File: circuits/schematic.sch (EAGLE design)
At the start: 38 parts, among them IC1 MEGA8-P, IC2 MAX481CPA, J1 AVR_SPI_PRG_6PTH

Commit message: Circuit layout v1.
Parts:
- added R14, R15, R16, R17: (no value), SparkFun-Passives:RESISTORPTH-1/4W
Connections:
- removed net N$14: IC1.PB2(SS/OC1B), R4.1
- removed net N$37: IC1.PD6(AIN0), JP2.6
- removed net N$38: R11.2, U$12.B
- removed net N$44: IC1.PC4(ADC4/SDA), R12.1
- removed net N$46: IC1.PD7(AIN1), JP4.6
- removed net N$49: IC1.PC3(ADC3), R11.1
- new net N$50: IC1.PC5(ADC5/SCL), R16.1
- new net N$51: JP4.3, U$12.C
- new net N$52: JP4.5, U$13.C
- new net N$53: JP4.4, U$14.C
- new net N$54: IC1.PB3(MOSI/OC2), J1.4, R3.1
- new net N$55: IC1.PB4(MISO), J1.1, R4.1
- net GND: now also J1.6, R13.2, R17.2, R2.2, R9.2, U$10.E, U$11.E, U$12.E, U$13.E, U$14.E, U$3.E, U$4.E, U$5.E, U$6.E, U$7.E, U$8.E, U$9.E; no longer JP1.1, JP1.2, JP2.1, JP2.2, JP3.1, JP3.2, JP4.1, JP4.2
- net N$10: now also JP1.4, U$8.C; no longer JP3.5, U$4.E
- net N$11: now also IC1.PC4(ADC4/SDA), R15.1; no longer JP3.4, U$5.E
- net N$12: now also R5.1; no longer R2.1
- net N$13: now also R6.1; no longer R3.1
- net N$15: now also JP1.6, R2.1; no longer JP3.6
- net N$21: now also IC1.PD5(T1), JP2.6, R9.1; no longer JP1.3, U$6.E
- net N$23: now also R3.2, U$3.B; no longer JP1.5, U$7.E
- net N$24: now also R4.2, U$4.B; no longer JP1.4, U$8.E
- net N$25: now also U$5.B; no longer U$9.B
- net N$26: now also IC1.PB5(SCK), J1.3, R8.1; no longer IC1.PB4(MISO), R6.1
- net N$27: now also IC1.PB2(SS/OC1B); no longer IC1.PB5(SCK)
- net N$28: now also JP2.3, U$3.C; no longer R4.2, U$5.B
- net N$29: now also JP2.5, U$4.C; no longer IC1.PD5(T1), JP1.6
- net N$3: now also IC1.PC3(ADC3), R14.1; no longer R2.2, U$3.B
- net N$30: now also JP2.4, U$5.C; no longer R9.2, U$10.B
- net N$31: now also IC1.PD6(AIN0), JP3.6, R13.1; no longer R10.2, U$11.B
- net N$32: now also R10.2, U$9.B; no longer JP2.3, U$9.E
- net N$33: now also R11.2, U$10.B; no longer JP2.5, U$10.E
- net N$34: now also R12.2, U$11.B; no longer JP2.4, U$11.E
- net N$35: now also R11.1; no longer R9.1
- net N$36: now also R12.1; no longer R10.1
- net N$39: now also JP3.3, U$9.C; no longer R12.2, U$13.B
- net N$40: now also JP3.5, U$10.C; no longer R13.2, U$14.B
- net N$41: now also JP3.4, U$11.C; no longer JP4.3, U$12.E
- net N$42: now also IC1.PD7(AIN1), JP4.6, R17.1; no longer JP4.5, U$13.E
- net N$43: now also R14.2, U$12.B; no longer JP4.4, U$14.E
- net N$45: now also R15.2, U$13.B; no longer IC1.PC5(ADC5/SCL), R13.1
- net N$47: now also R16.2, U$14.B; no longer IC1.PB3(MOSI/OC2), R5.1
- net N$48: now also R10.1; no longer R8.1
- net N$6: now also JP1.3, U$6.C; no longer R3.2, U$4.B
- net N$9: now also JP1.5, U$7.C; no longer JP3.3, U$3.E
- net VCC: now also JP1.1, JP1.2, JP2.1, JP2.2, JP3.1, JP3.2, JP4.1, JP4.2; no longer U$10.C, U$11.C, U$12.C, U$13.C, U$14.C, U$3.C, U$4.C, U$5.C, U$6.C, U$7.C, U$8.C, U$9.C
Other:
- moved on the sheet: JP1, JP2, JP3, JP4, R10, R11, R12, R13, R2, R3, R4, R5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

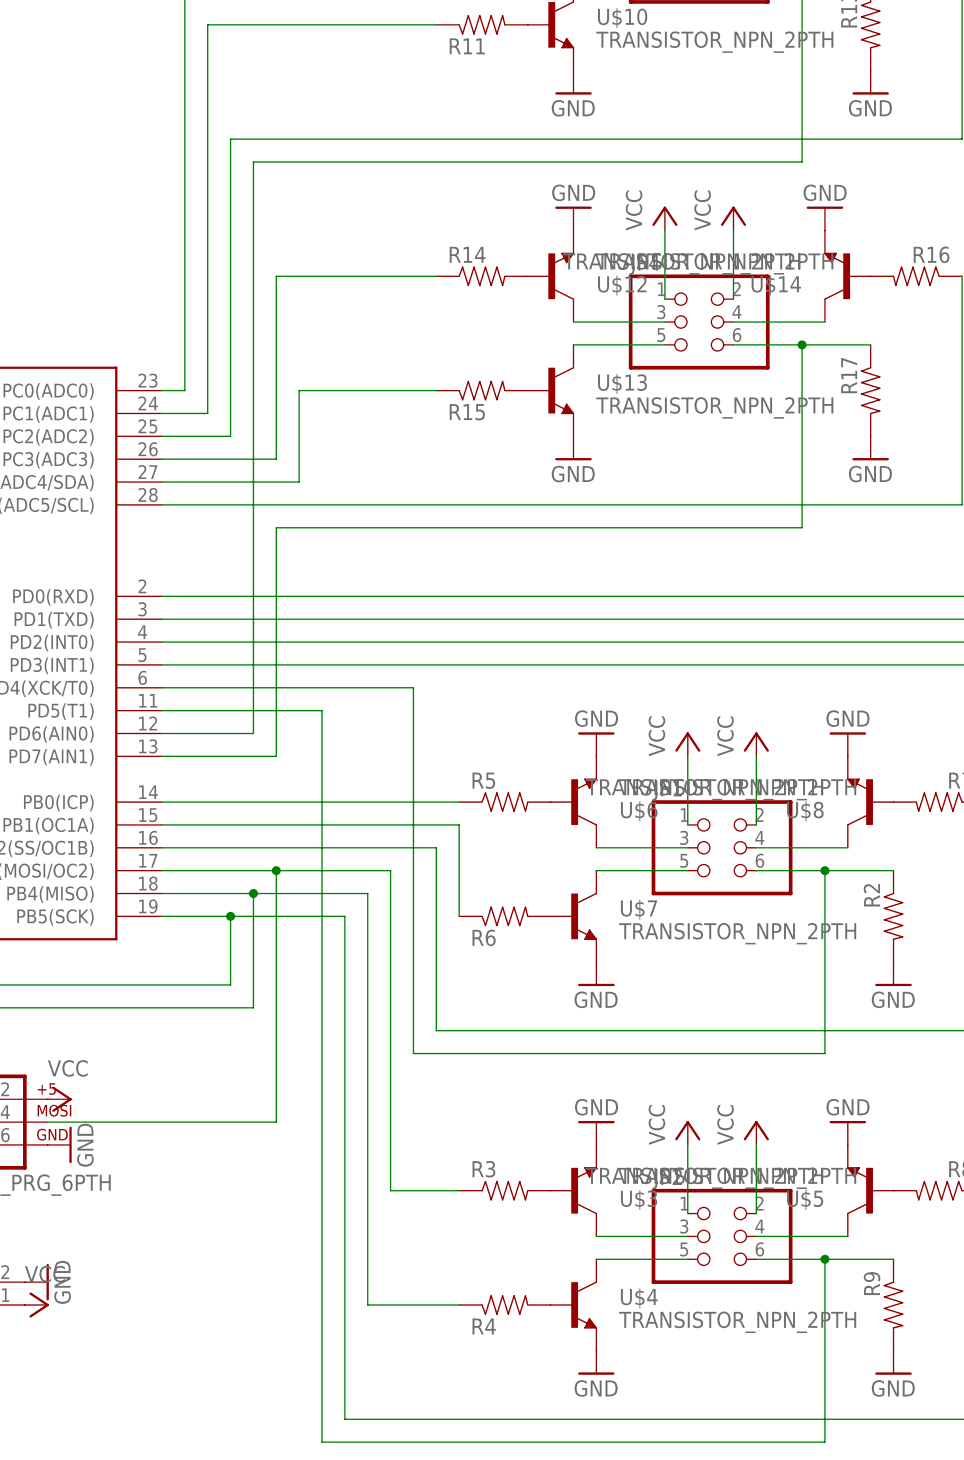
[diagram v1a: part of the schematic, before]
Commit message: Inverted switch order.
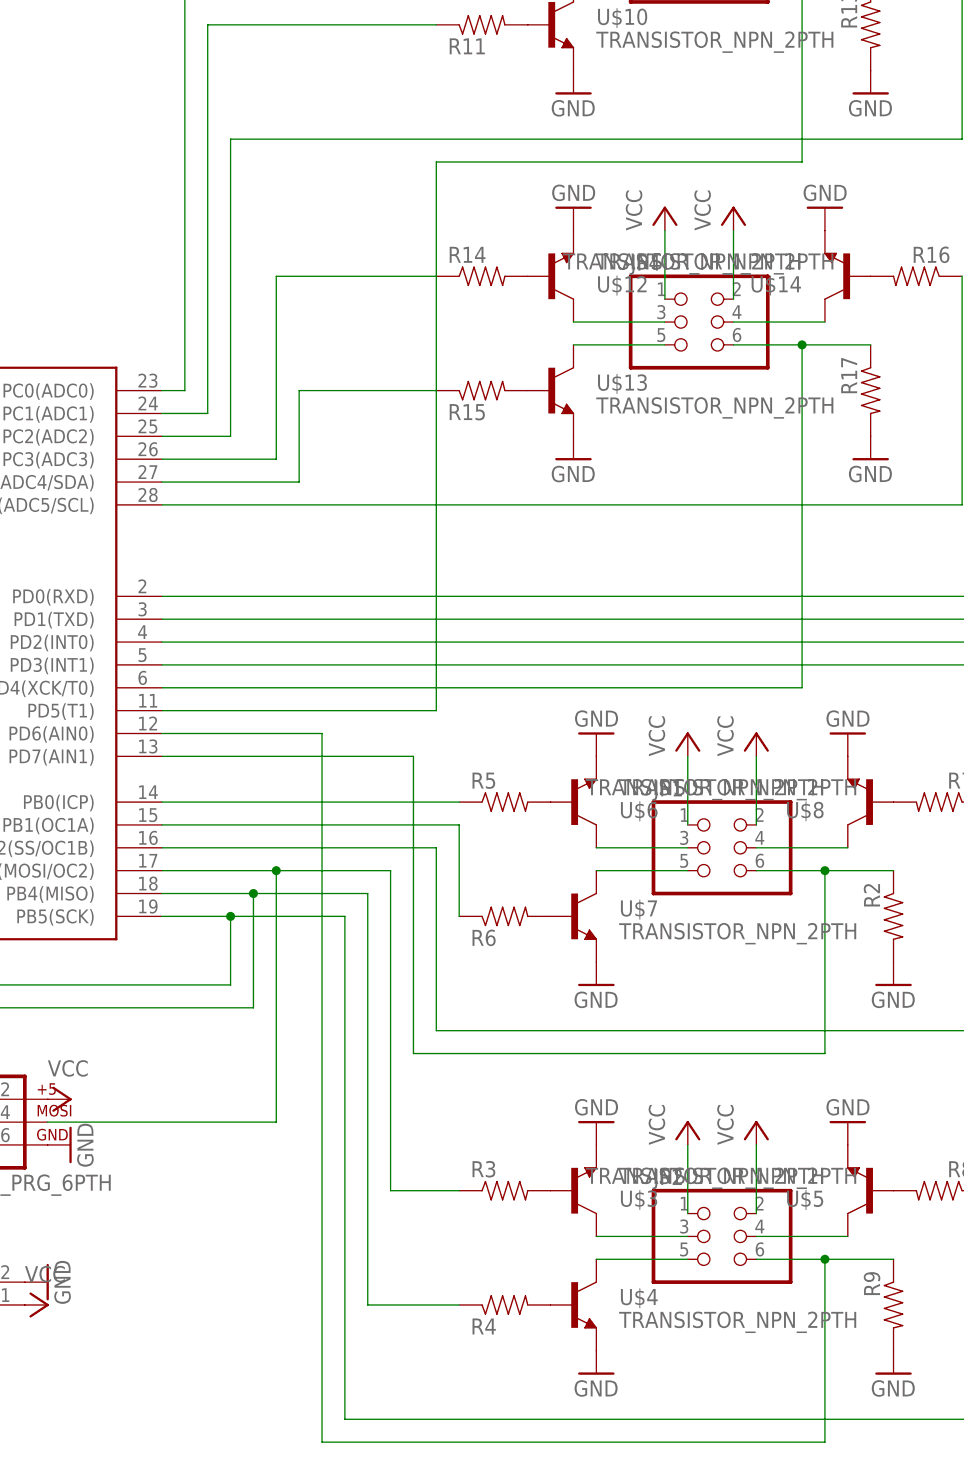
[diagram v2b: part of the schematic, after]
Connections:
- removed net N$15: IC1.PD4(XCK/T0), JP1.6, R2.1
- new net N$14: IC1.PD7(AIN1), JP1.6, R2.1
- net N$21: now also IC1.PD6(AIN0); no longer IC1.PD5(T1)
- net N$31: now also IC1.PD5(T1); no longer IC1.PD6(AIN0)
- net N$42: now also IC1.PD4(XCK/T0); no longer IC1.PD7(AIN1)
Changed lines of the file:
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@@
 <grid distance="0.1" unitdist="inch" unit="inch" style="lines" multiple="1" display="no" altdistance="0.01" altunitdist="inch" altunit="inch"/>
 <layers>
-<layer number="1" name="Top" color="4" fill="1" visible="no" active="no"/>
-<layer number="16" name="Bottom" color="1" fill="1" visible="no" active="no"/>
-<layer number="17" name="Pads" color="2" fill="1" visible="no" active="no"/>
-<layer number="18" name="Vias" color="2" fill="1" visible="no" active="no"/>
-<layer number="19" name="Unrouted" color="6" fill="1" visible="no" active="no"/>
-<layer number="20" name="Dimension" color="15" fill="1" visible="no" active="no"/>
-<layer number="21" name="tPlace" color="7" fill="1" visible="no" active="no"/>
-<layer number="22" name="bPlace" color="7" fill="1" visible="no" active="no"/>
-<layer number="23" name="tOrigins" color="15" fill="1" visible="no" active="no"/>
-<layer number="24" name="bOrigins" color="15" fill="1" visible="no" active="no"/>
-<layer number="25" name="tNames" color="7" fill="1" visible="no" active="no"/>
-<layer number="26" name="bNames" color="7" fill="1" visible="no" active="no"/>
-<layer number="27" name="tValues" color="7" fill="1" visible="no" active="no"/>
-<layer number="28" name="bValues" color="7" fill="1" visible="no" active="no"/>
+<layer number="1" name="Top" color="4" fill="1" visible="yes" active="no"/>
+<layer number="16" name="Bottom" color="1" fill="1" visible="yes" active="no"/>
+<layer number="17" name="Pads" color="2" fill="1" visible="yes" active="no"/>
+<layer number="18" name="Vias" color="2" fill="1" visible="yes" active="no"/>
+<layer number="19" name="Unrouted" color="6" fill="1" visible="yes" active="no"/>
+<layer number="20" name="Dimension" color="15" fill="1" visible="yes" active="no"/>
+<layer number="21" name="tPlace" color="7" fill="1" visible="yes" active="no"/>
+<layer number="22" name="bPlace" color="7" fill="1" visible="yes" active="no"/>
+<layer number="23" name="tOrigins" color="15" fill="1" visible="yes" active="no"/>
+<layer number="24" name="bOrigins" color="15" fill="1" visible="yes" active="no"/>
+<layer number="25" name="tNames" color="7" fill="1" visible="yes" active="no"/>
+<layer number="26" name="bNames" color="7" fill="1" visible="yes" active="no"/>
+<layer number="27" name="tValues" color="7" fill="1" visible="yes" active="no"/>
+<layer number="28" name="bValues" color="7" fill="1" visible="yes" active="no"/>
 <layer number="29" name="tStop" color="7" fill="3" visible="no" active="no"/>
 <layer number="30" name="bStop" color="7" fill="6" visible="no" active="no"/>
@@
 <layer number="35" name="tGlue" color="7" fill="4" visible="no" active="no"/>
 <layer number="36" name="bGlue" color="7" fill="5" visible="no" active="no"/>
-<layer number="37" name="tTest" color="7" fill="1" visible="no" active="no"/>
-<layer number="38" name="bTest" color="7" fill="1" visible="no" active="no"/>
+<layer number="37" name="tTest" color="7" fill="1" visible="yes" active="no"/>
+<layer number="38" name="bTest" color="7" fill="1" visible="yes" active="no"/>
 <layer number="39" name="tKeepout" color="4" fill="11" visible="no" active="no"/>
 <layer number="40" name="bKeepout" color="1" fill="11" visible="no" active="no"/>
@@
 <layer number="44" name="Drills" color="7" fill="1" visible="no" active="no"/>
 <layer number="45" name="Holes" color="7" fill="1" visible="no" active="no"/>
-<layer number="46" name="Milling" color="3" fill="1" visible="no" active="no"/>
-<layer number="47" name="Measures" color="7" fill="1" visible="no" active="no"/>
-<layer number="48" name="Document" color="7" fill="1" visible="no" active="no"/>
-<layer number="49" name="Reference" color="7" fill="1" visible="no" active="no"/>
-<layer number="50" name="dxf" color="7" fill="1" visible="no" active="no"/>
-<layer number="51" name="tDocu" color="7" fill="1" visible="no" active="no"/>
-<layer number="52" name="bDocu" color="7" fill="1" visible="no" active="no"/>
-<layer number="53" name="tGND_GNDA" color="7" fill="9" visible="no" active="no"/>
-<layer number="54" name="bGND_GNDA" color="1" fill="9" visible="no" active="no"/>
-<layer number="56" name="wert" color="7" fill="1" visible="no" active="no"/>
+<layer number="46" name="Milling" color="3" fill="1" visible="yes" active="no"/>
+<layer number="47" name="Measures" color="7" fill="1" visible="yes" active="no"/>
+<layer number="48" name="Document" color="7" fill="1" visible="yes" active="no"/>
+<layer number="49" name="Reference" color="7" fill="1" visible="yes" active="no"/>
+<layer number="50" name="dxf" color="7" fill="1" visible="yes" active="no"/>
+<layer number="51" name="tDocu" color="7" fill="1" visible="yes" active="no"/>
+<layer number="52" name="bDocu" color="7" fill="1" visible="yes" active="no"/>
+<layer number="53" name="tGND_GNDA" color="7" fill="9" visible="yes" active="no"/>
+<layer number="54" name="bGND_GNDA" color="1" fill="9" visible="yes" active="no"/>
+<layer number="56" name="wert" color="7" fill="1" visible="yes" active="no"/>
 <layer number="91" name="Nets" color="2" fill="1" visible="yes" active="yes"/>
 <layer number="92" name="Busses" color="1" fill="1" visible="yes" active="yes"/>
@@
 </segment>
 </net>
-<net name="N$15" class="0">
-<segment>
-<pinref part="IC1" gate="G$1" pin="PD4(XCK/T0)"/>
-<wire x1="99.06" y1="40.64" x2="71.12" y2="40.64" width="0.1524" layer="91"/>
-<wire x1="99.06" y1="40.64" x2="99.06" y2="0" width="0.1524" layer="91"/>
-<pinref part="JP1" gate="A" pin="6"/>
-<pinref part="R2" gate="G$1" pin="1"/>
-<wire x1="137.16" y1="20.32" x2="144.78" y2="20.32" width="0.1524" layer="91"/>
-<wire x1="144.78" y1="20.32" x2="152.4" y2="20.32" width="0.1524" layer="91"/>
-<wire x1="144.78" y1="20.32" x2="144.78" y2="0" width="0.1524" layer="91"/>
-<junction x="144.78" y="20.32"/>
-<wire x1="99.06" y1="0" x2="144.78" y2="0" width="0.1524" layer="91"/>
-</segment>
-</net>
 <net name="N$1" class="0">
 <segment>
@@
 <wire x1="144.78" y1="-22.86" x2="144.78" y2="-43.18" width="0.1524" layer="91"/>
 <junction x="144.78" y="-22.86"/>
+<pinref part="IC1" gate="G$1" pin="PD6(AIN0)"/>
+<wire x1="71.12" y1="35.56" x2="88.9" y2="35.56" width="0.1524" layer="91"/>
+<wire x1="88.9" y1="35.56" x2="88.9" y2="-43.18" width="0.1524" layer="91"/>
 <wire x1="88.9" y1="-43.18" x2="144.78" y2="-43.18" width="0.1524" layer="91"/>
-<wire x1="88.9" y1="-43.18" x2="88.9" y2="38.1" width="0.1524" layer="91"/>
-<pinref part="IC1" gate="G$1" pin="PD5(T1)"/>
-<wire x1="88.9" y1="38.1" x2="71.12" y2="38.1" width="0.1524" layer="91"/>
 </segment>
 </net>
@@
 <wire x1="142.24" y1="119.38" x2="142.24" y2="99.06" width="0.1524" layer="91"/>
 <junction x="142.24" y="119.38"/>
-<wire x1="81.28" y1="99.06" x2="142.24" y2="99.06" width="0.1524" layer="91"/>
-<wire x1="81.28" y1="99.06" x2="81.28" y2="35.56" width="0.1524" layer="91"/>
-<pinref part="IC1" gate="G$1" pin="PD6(AIN0)"/>
-<wire x1="81.28" y1="35.56" x2="71.12" y2="35.56" width="0.1524" layer="91"/>
+<pinref part="IC1" gate="G$1" pin="PD5(T1)"/>
+<wire x1="71.12" y1="38.1" x2="101.6" y2="38.1" width="0.1524" layer="91"/>
+<wire x1="101.6" y1="38.1" x2="101.6" y2="99.06" width="0.1524" layer="91"/>
+<wire x1="101.6" y1="99.06" x2="142.24" y2="99.06" width="0.1524" layer="91"/>
 </segment>
 </net>
@@
 <wire x1="134.62" y1="78.74" x2="142.24" y2="78.74" width="0.1524" layer="91"/>
 <wire x1="142.24" y1="78.74" x2="149.86" y2="78.74" width="0.1524" layer="91"/>
-<wire x1="142.24" y1="78.74" x2="142.24" y2="58.42" width="0.1524" layer="91"/>
+<wire x1="142.24" y1="78.74" x2="142.24" y2="40.64" width="0.1524" layer="91"/>
 <junction x="142.24" y="78.74"/>
-<wire x1="83.82" y1="58.42" x2="142.24" y2="58.42" width="0.1524" layer="91"/>
-<wire x1="83.82" y1="58.42" x2="83.82" y2="33.02" width="0.1524" layer="91"/>
-<pinref part="IC1" gate="G$1" pin="PD7(AIN1)"/>
-<wire x1="83.82" y1="33.02" x2="71.12" y2="33.02" width="0.1524" layer="91"/>
+<pinref part="IC1" gate="G$1" pin="PD4(XCK/T0)"/>
+<wire x1="71.12" y1="40.64" x2="142.24" y2="40.64" width="0.1524" layer="91"/>
 </segment>
 </net>
@@
 </segment>
 </net>
+<net name="N$14" class="0">
+<segment>
+<pinref part="R2" gate="G$1" pin="1"/>
+<pinref part="JP1" gate="A" pin="6"/>
+<wire x1="137.16" y1="20.32" x2="144.78" y2="20.32" width="0.1524" layer="91"/>
+<wire x1="144.78" y1="20.32" x2="152.4" y2="20.32" width="0.1524" layer="91"/>
+<junction x="144.78" y="20.32"/>
+<wire x1="144.78" y1="20.32" x2="144.78" y2="0" width="0.1524" layer="91"/>
+<pinref part="IC1" gate="G$1" pin="PD7(AIN1)"/>
+<wire x1="71.12" y1="33.02" x2="99.06" y2="33.02" width="0.1524" layer="91"/>
+<wire x1="99.06" y1="33.02" x2="99.06" y2="0" width="0.1524" layer="91"/>
+<wire x1="99.06" y1="0" x2="144.78" y2="0" width="0.1524" layer="91"/>
+</segment>
+</net>
